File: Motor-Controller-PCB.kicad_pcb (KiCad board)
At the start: 2 copper layers, 12 parts, among them Q1 AO3401A

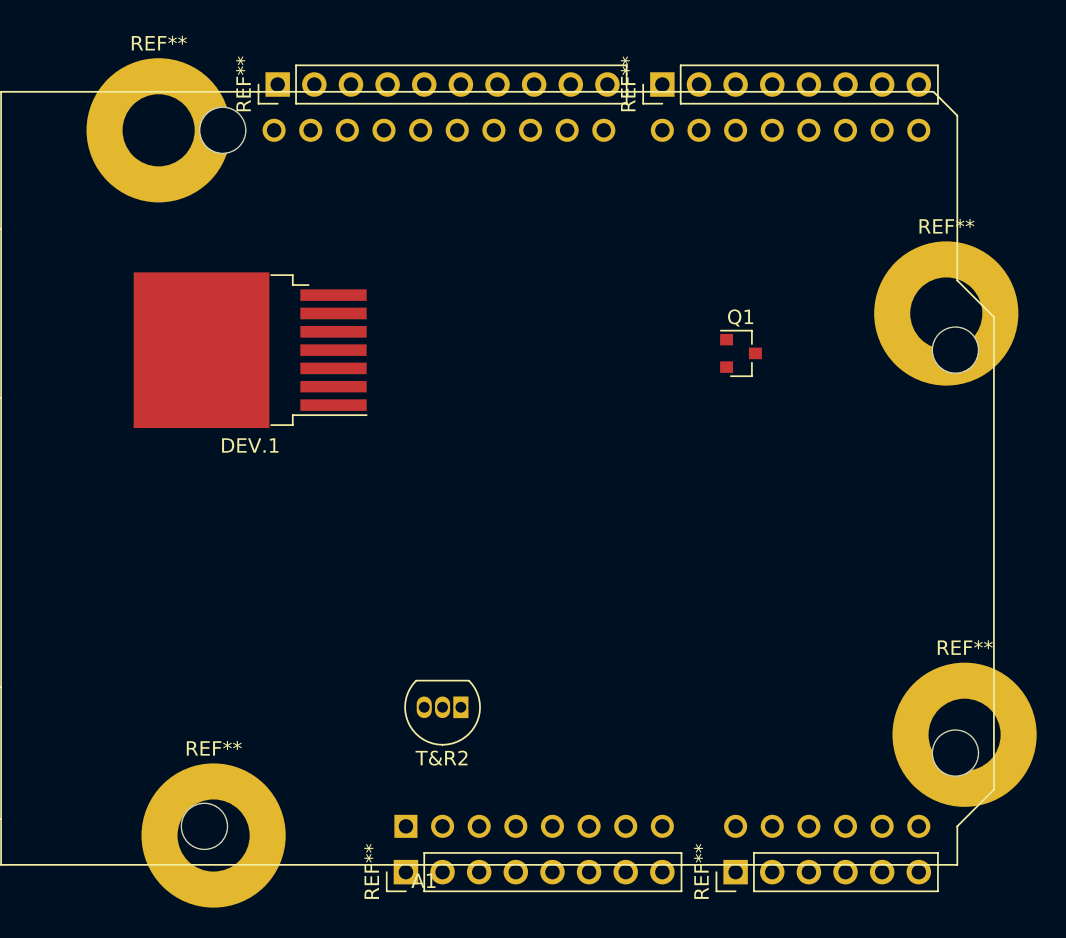
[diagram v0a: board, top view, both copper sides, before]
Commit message: Better board outline and 4mm through holes
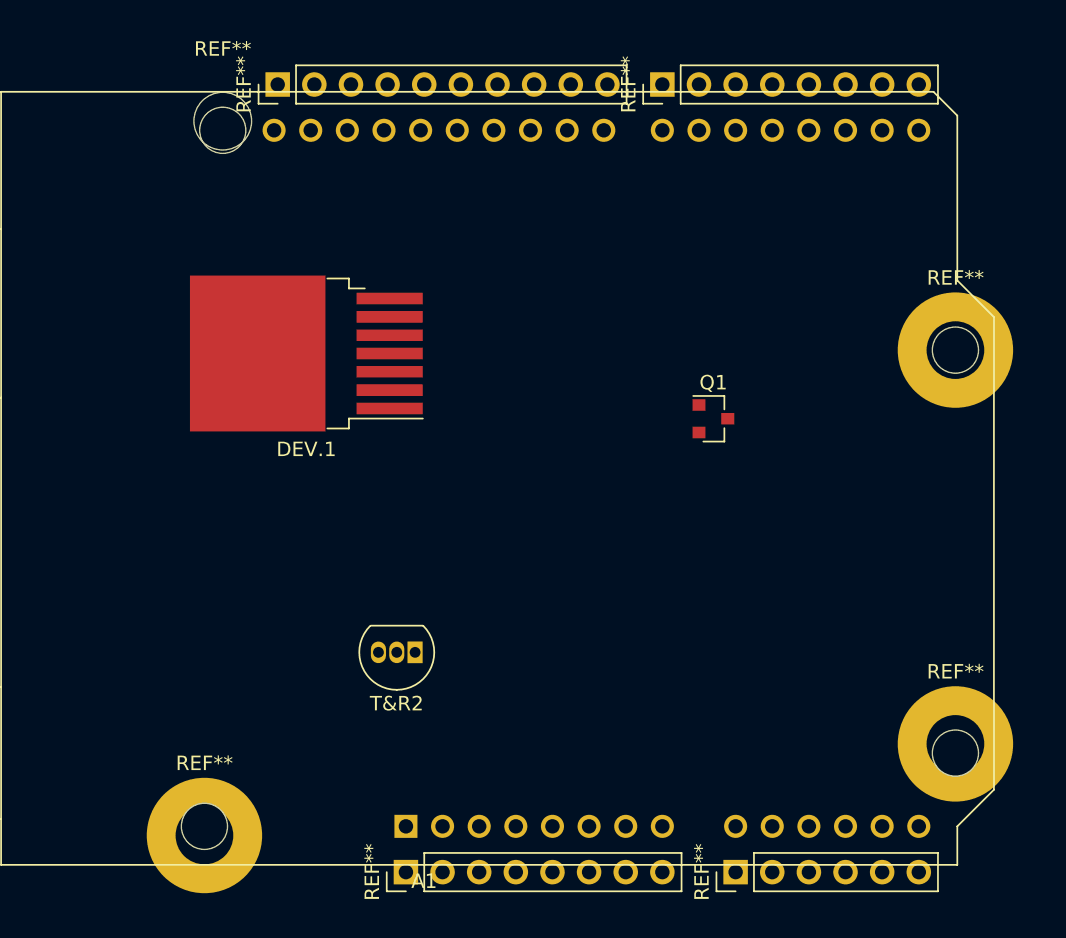
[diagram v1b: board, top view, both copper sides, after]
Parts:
- removed the REF** at (154.3, 31.1)
- removed the REF** at (158.1, 80.0)
- removed the REF** at (210.2, 73.0)
- removed the REF** at (208.9, 43.8)
- added REF**: MountingHole_4mm, MountingHole:MountingHole_4mm, F.Cu at (158.8, 30.5)
- added REF**: MountingHole_4mm_Pad, MountingHole:MountingHole_4mm_Pad, F.Cu at (157.5, 80.0)
- added REF**: MountingHole_4mm_Pad, MountingHole:MountingHole_4mm_Pad, F.Cu at (209.6, 73.7)
- added REF**: MountingHole_4mm_Pad, MountingHole:MountingHole_4mm_Pad, F.Cu at (209.6, 46.4)
- moved T&R2 4.96 mm to (172.1, 67.3)
- moved Q1 4.92 mm to (192.8, 51.1)
- moved DEV.1 3.90 mm to (164.6, 46.6)

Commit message: layouting
almost done
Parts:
- removed REF**: MountingHole_4mm, MountingHole:MountingHole_4mm
- removed REF** (x3): MountingHole_4mm_Pad, MountingHole:MountingHole_4mm_Pad
- removed REF**: PinHeader_1x06_P2.54mm_Vertical, Connector_PinHeader_2.54mm:PinHeader_1x06_P2.54mm_Vertical
- removed REF** (x2): PinHeader_1x08_P2.54mm_Vertical, Connector_PinHeader_2.54mm:PinHeader_1x08_P2.54mm_Vertical
- removed REF**: PinHeader_1x10_P2.54mm_Vertical, Connector_PinHeader_2.54mm:PinHeader_1x10_P2.54mm_Vertical
- added C10: 1nF, Capacitor_SMD:C_0805_2012Metric, B.Cu at (132.0, 102.0)
- added C11: 100nF, Capacitor_SMD:C_0805_2012Metric, B.Cu at (145.0, 116.0)
- added C12: 100uF, Capacitor_SMD:C_0805_2012Metric, B.Cu at (140.0, 96.0)
- added C14: 100nF, Capacitor_SMD:C_0805_2012Metric, B.Cu at (166.0, 94.0)
- added C4: 50V & 1500u, Capacitor_THT:CP_Radial_D18.0mm_P7.50mm, F.Cu at (163.5, 105.0)
- added C5: 220nF, Capacitor_SMD:C_0805_2012Metric, B.Cu at (145.3, 92.9)
- added C6: 220nF, Capacitor_SMD:C_0805_2012Metric, B.Cu at (156.7, 92.9)
- added D2: ZMY39, Diode_SMD:D_MELF, B.Cu at (171.0, 94.0)
- added D3: BZV55-C10, Diode_SMD:D_MiniMELF, B.Cu at (145.0, 106.0)
- added R1: 10K, Resistor_SMD:R_0805_2012Metric, B.Cu at (174.0, 76.0)
- added R12: 4.7K, Resistor_SMD:R_0805_2012Metric, B.Cu at (127.0, 86.0)
- added R13: 10K, Resistor_SMD:R_0805_2012Metric, B.Cu at (127.0, 109.0)
- added R14: 1K, Resistor_SMD:R_0805_2012Metric, B.Cu at (138.0, 116.0)
- added R15: 10K, Resistor_SMD:R_0805_2012Metric, B.Cu at (143.0, 101.0)
- added R5: 10K, Resistor_SMD:R_0805_2012Metric, B.Cu at (182.0, 85.0)
- added R7: 1K, Resistor_SMD:R_0805_2012Metric, B.Cu at (127.0, 102.1)
- added R9: 470, Resistor_SMD:R_0805_2012Metric, B.Cu at (141.5, 116.0)
- A1, DEV.1, Q1, T&R2: moved to B.Cu
- moved Q1 74.1 mm to (138.0, 101.0), turned to 90 degrees
- moved A1 58.2 mm to (184.2, 123.5), turned to 180 degrees
- moved T&R2 43.0 mm to (132.0, 83.0), turned to 90 degrees
- moved DEV.1 37.4 mm to (154.9, 82.7)
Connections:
- net Net-(C5-Pad2) renamed OUT_1
- DEV.1 pad 7: Net-(C1-Pad2) -> Net-(C14-Pad1)
- Q1 pad 2: GNDREF -> Net-(C14-Pad1)
- Q1 pad 3: VS -> VBAT
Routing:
- net GNDREF: track 0.00 -> 257.0 mm
- net Net-(A1-Pad27): track 0.00 -> 192.0 mm
- net 5V_ARDUINO: track 0.00 -> 101.6 mm
- net Net-(A1-Pad9): track 0.00 -> 100.6 mm
- net Net-(C14-Pad1): track 0.00 -> 81.8 mm
- net Net-(C11-Pad1): track 0.00 -> 73.8 mm
- net Net-(A1-Pad18): track 0.00 -> 50.9 mm
- net OUT_1: track 0.00 -> 33.1 mm
- net Net-(A1-Pad12): track 0.00 -> 30.7 mm
- net VBAT: track 0.00 -> 24.8 mm
- net Net-(DEV.1-Pad3): track 0.00 -> 24.0 mm
- net Net-(DEV.1-Pad2): track 0.00 -> 14.7 mm
- net Net-(D3-Pad2): track 0.00 -> 9.22 mm
- net Net-(R12-Pad1): track 0.00 -> 6.98 mm
- net Net-(A1-Pad31): track 0.00 -> 2.54 mm
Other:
- rule pad_to_mask_clearance: 0 -> 0.0508
- rule via_min_size: 0.4 -> 0.5

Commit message: Update Motor-Controller-PCB.kicad_pcb
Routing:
- added copper zone on B.Cu, net GNDREF
- added copper zone on F.Cu, net GNDREF

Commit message: board
giant green circles
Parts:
- added Q1: TO-252-2, Package_TO_SOT_SMD:TO-252-2, B.Cu at (167.6, 83.4)
- added REF**: Giant_Green_Circle, Motor-Controller-PCB:Giant_Green_Circle, F.Cu at (123.9, 102.8)
- added REF**: Giant_Green_Circle, Motor-Controller-PCB:Giant_Green_Circle, F.Cu at (178.6, 79.0)
- added REF**: Giant_Green_Circle, Motor-Controller-PCB:Giant_Green_Circle, F.Cu at (175.8, 118.2)
- added REF**: Giant_Green_Circle, Motor-Controller-PCB:Giant_Green_Circle, F.Cu at (124.2, 82.6)
- C6: moved to F.Cu
- moved C11 29.0 mm to (149.6, 87.4), turned to 0 degrees
- moved R9 27.6 mm to (149.5, 89.6), turned to 180 degrees
- moved C4 25.4 mm to (149.8, 83.6), turned to 0 degrees
- moved R7 23.8 mm to (149.5, 94.2), turned to 180 degrees
- moved C12 23.1 mm to (121.5, 109.7)
- moved C10 20.2 mm to (149.4, 91.8), turned to 180 degrees
- moved R5 19.2 mm to (165.2, 75.8)
- moved C6 17.5 mm to (142.0, 83.4)
- moved DEV.1 17.3 mm to (138.2, 87.0)
- moved T&R2 12.7 mm to (134.7, 95.4), turned to 0 degrees
- moved C5 9.31 mm to (150.2, 100.8)
- moved R12 2.93 mm to (125.7, 88.6)
- moved R1 2.00 mm to (172.0, 75.9)
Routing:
- net GNDREF: track 257.0 -> 52.4 mm, vias 0 -> 6
- net Net-(C11-Pad1): track 73.8 -> 7.39 mm
- net 5V_ARDUINO: track 101.6 -> 68.3 mm
- net OUT_1: track 33.1 -> 8.29 mm
- net Net-(DEV.1-Pad3): track 24.0 -> 0.00 mm
- net Net-(DEV.1-Pad2): track 14.7 -> 0.00 mm
- net VBAT: track 24.8 -> 10.7 mm
- net Net-(A1-Pad9): track 100.6 -> 92.7 mm
- net Net-(R12-Pad1): track 6.98 -> 0.00 mm
- net Net-(A1-Pad18): track 50.9 -> 46.1 mm
- net Net-(C14-Pad1): track 81.8 -> 86.3 mm
- net Net-(A1-Pad27): track 192.0 -> 190.5 mm
- removed copper zone on B.Cu, net GNDREF
- removed copper zone on F.Cu, net GNDREF

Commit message: layouting
layouting
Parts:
- removed the Q1 at (167.6, 83.4)
- removed the Q1 at (138.0, 101.0)
- removed the REF** at (123.9, 102.8)
- removed the REF** at (178.6, 79.0)
- removed the REF** at (175.8, 118.2)
- removed the REF** at (124.2, 82.6)
- added Q1: IPD90P04P4L, Motor-Controller-PCB:TO-252-3_TabPin2, B.Cu at (170.2, 90.1)
- added REF**: Giant_Green_Circle, Motor-Controller-PCB:Giant_Green_Circle, F.Cu at (122.8, 105.2)
- added REF**: Giant_Green_Circle, Motor-Controller-PCB:Giant_Green_Circle, F.Cu at (175.8, 115.5)
- added REF**: Giant_Green_Circle, Motor-Controller-PCB:Giant_Green_Circle, F.Cu at (177.5, 80.0)
- added REF**: Giant_Green_Circle, Motor-Controller-PCB:Giant_Green_Circle, F.Cu at (124.6, 84.1)
- moved C12 56.2 mm to (176.9, 118.9), turned to 0 degrees
- moved R1 40.9 mm to (131.1, 74.9), turned to 180 degrees
- moved R15 30.4 mm to (173.4, 100.3), turned to 0 degrees
- moved R13 28.9 mm to (154.9, 116.5)
- moved C5 28.0 mm to (122.9, 94.7), turned to 90 degrees
- moved D3 27.1 mm to (170.8, 97.7), turned to 0 degrees
- moved R12 25.3 mm to (136.9, 111.3), turned to 0 degrees
- moved C14 15.9 mm to (160.6, 79.0)
- moved D2 15.0 mm to (164.4, 80.5)
- moved R14 12.5 mm to (125.5, 117.3), turned to 90 degrees
- moved R5 12.0 mm to (153.5, 78.5), turned to 270 degrees
- moved A1 0.25 mm to (184.0, 123.5)
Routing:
- net Net-(A1-Pad27): track 190.5 -> 5.29 mm
- net Net-(A1-Pad18): track 46.1 -> 3.77 mm
- net GNDREF: track 52.4 -> 83.5 mm, vias 6 -> 12
- net VBAT: track 10.7 -> 37.6 mm
- net Net-(A1-Pad9): track 92.7 -> 68.4 mm
- net Net-(DEV.1-Pad2): track 0.00 -> 22.3 mm
- net Net-(R12-Pad1): track 0.00 -> 15.9 mm
- net Net-(DEV.1-Pad3): track 0.00 -> 14.3 mm
- net Net-(A1-Pad12): track 30.7 -> 37.4 mm
- net Net-(C14-Pad1): track 86.3 -> 89.6 mm
- net Net-(D3-Pad2): track 9.22 -> 6.03 mm
- net OUT_1: track 8.29 -> 10.5 mm
- net 5V_ARDUINO: track 68.3 -> 69.0 mm
- added copper zone on B.Cu, net GNDREF
- added copper zone on F.Cu, net GNDREF
- added copper zone on B.Cu, net Net-(C14-Pad1)
- added copper zone on B.Cu, net OUT_1
- added copper zone on F.Cu, net OUT_1
- added copper zone on B.Cu, net VBAT
- added copper zone on F.Cu, net VBAT

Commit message: layouting
layouting
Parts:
- C12: footprint Capacitor_SMD:C_0805_2012Metric -> Capacitor_SMD:CP_Elec_10x10; moved to F.Cu
- C6: moved to B.Cu
- D2: value ZMY39 -> 1N4754A; footprint Diode_SMD:D_MELF -> Diode_THT:D_DO-41_SOD81_P10.16mm_Horizontal; moved to F.Cu
- moved C12 28.1 mm to (178.7, 90.8), turned to 90 degrees
- moved C4 14.3 mm to (149.3, 97.9)
- moved C6 8.41 mm to (149.9, 86.2)
- moved D2 4.65 mm to (164.4, 75.8)
- moved T&R2 3.20 mm to (134.7, 98.6)
- moved C11 0.96 mm to (149.9, 88.3)
- moved R9 0.89 mm to (149.9, 90.4)
- moved C10 0.80 mm to (149.9, 92.4)
- moved R7 0.52 mm to (149.9, 94.5)
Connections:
- A1 pad 32: Net-(A1-Pad31) -> Net-(A1-Pad32)
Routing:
- net Net-(C14-Pad1): track 89.6 -> 58.6 mm
- net GNDREF: track 83.5 -> 59.6 mm
- net Net-(R12-Pad1): track 15.9 -> 12.7 mm
- net Net-(A1-Pad9): track 68.4 -> 71.5 mm
- net OUT_1: track 10.5 -> 13.2 mm
- net Net-(A1-Pad31): track 2.54 -> 0.00 mm
- net Net-(C11-Pad1): track 7.39 -> 9.55 mm
- net VBAT: track 37.6 -> 35.6 mm

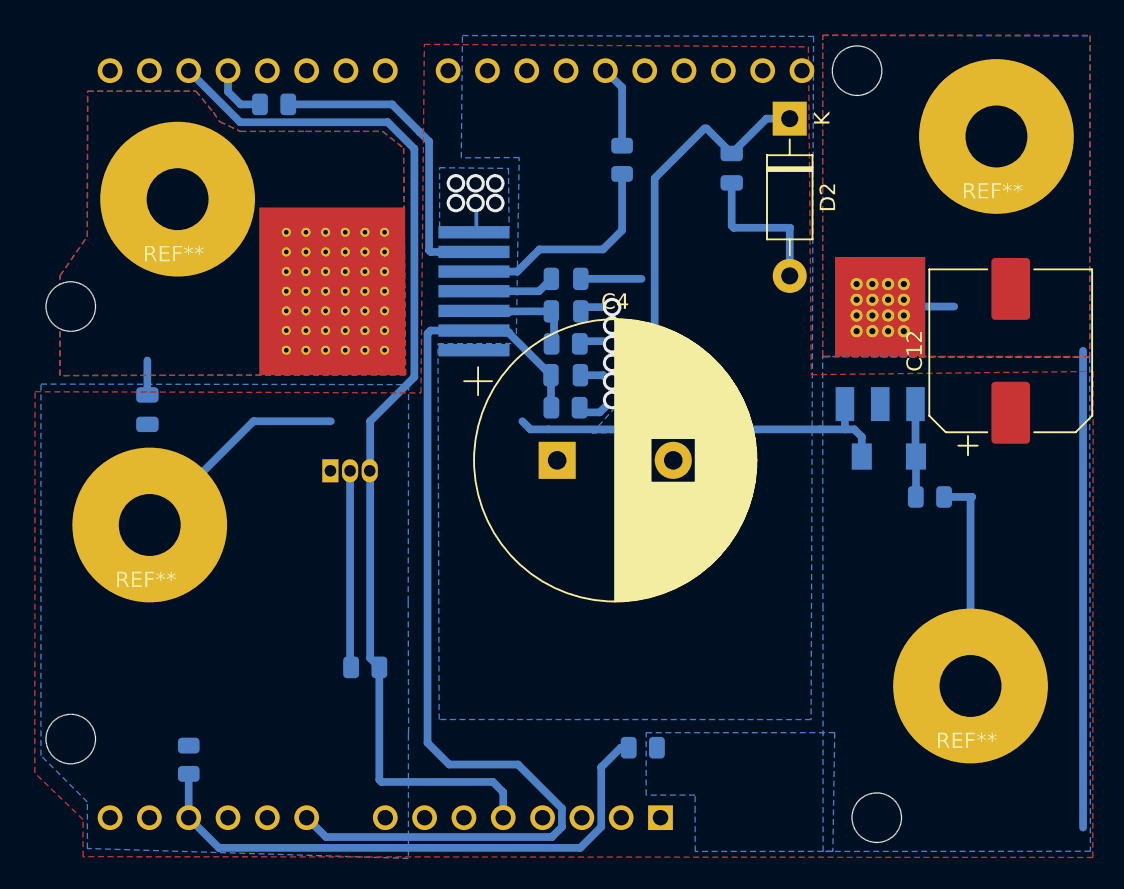
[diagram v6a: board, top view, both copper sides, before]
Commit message: New parts and schematic cleanup
Co-Authored-By: William <28985448+wzhouiup@users.noreply.github.com>
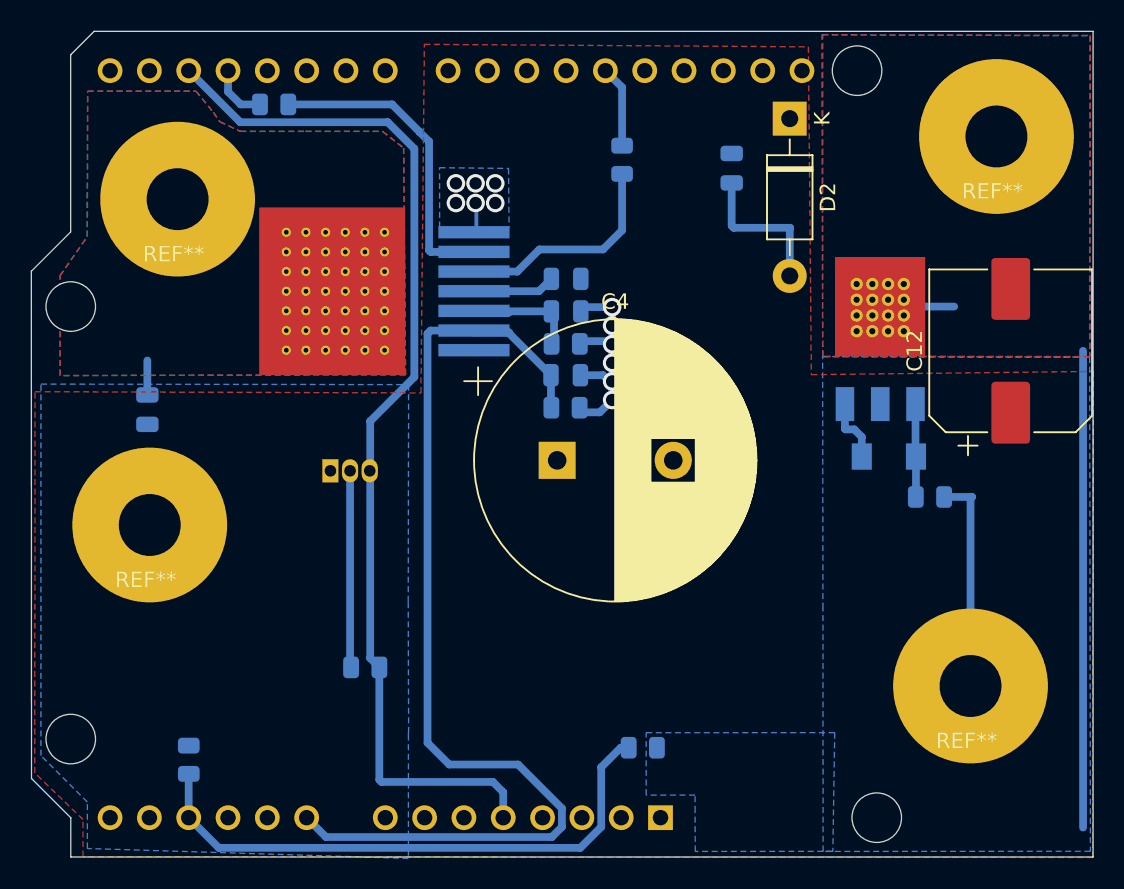
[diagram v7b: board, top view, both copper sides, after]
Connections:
- net GNDREF renamed GND
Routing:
- net Net-(C14-Pad1): track 58.6 -> 5.35 mm
- net GND: track 59.6 -> 45.1 mm
- removed copper zone on B.Cu, net Net-(C14-Pad1)
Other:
- board outline added: 68.6 x 53.3 mm
- net class Default: clearance 0.2 -> 0.1524; trace_width 0.25 -> 0.1524; via_dia 0.8 -> 0.508; via_drill 0.4 -> 0.254
- rule trace_clearance: 0.2 -> 0.1524
- rule trace_min: 0.2 -> 0.1524
- rule via_min_drill: 0.3 -> 0.254
- rule via_min_size: 0.5 -> 0.508

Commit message: layouting
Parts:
- removed C10: 1nF, Capacitor_SMD:C_0805_2012Metric
- removed C12: 100uF, Capacitor_SMD:CP_Elec_10x10
- removed DEV.1: BTN8982TA, Package_TO_SOT_SMD:TO-263-7_TabPin8
- removed R12: 4.7K, Resistor_SMD:R_0805_2012Metric
- removed R7: 1K, Resistor_SMD:R_0805_2012Metric
- removed R9: 470, Resistor_SMD:R_0805_2012Metric
- removed T&R2: DS18B20, Package_TO_SOT_THT:TO-92_Inline
- added C1: 10nF, Capacitor_SMD:C_0805_2012Metric_Pad1.18x1.45mm_HandSolder, B.Cu at (130.6, 117.5)
- added C11: 100nF, Capacitor_SMD:C_0805_2012Metric_Pad1.18x1.45mm_HandSolder, B.Cu at (149.4, 90.5)
- added C14: 100nF, Capacitor_SMD:C_0805_2012Metric_Pad1.18x1.45mm_HandSolder, B.Cu at (160.5, 86.6)
- added C2: 1µF, Capacitor_SMD:C_0805_2012Metric_Pad1.18x1.45mm_HandSolder, B.Cu at (160.9, 94.5)
- added C5: 220nF, Capacitor_SMD:C_0805_2012Metric_Pad1.18x1.45mm_HandSolder, B.Cu at (120.7, 94.8)
- added C6: 220nF, Capacitor_SMD:C_0805_2012Metric_Pad1.18x1.45mm_HandSolder, B.Cu at (149.9, 83.8)
- added C7: 100µF, Capacitor_SMD:CP_Elec_10x10, B.Cu at (168.3, 105.0)
- added D1: 10V, Diode_SMD:D_MiniMELF, B.Cu at (163.1, 97.7)
- added Q2: TJ200F04M3L, Motor-Controller-PCB:TO-220SM-3_TabPin2_ThermalVias, B.Cu at (161.0, 107.8)
- added Q3: TJ200F04M3L, Motor-Controller-PCB:TO-220SM-3_TabPin2_ThermalVias, B.Cu at (171.9, 95.1)
- added R2: 20k, Resistor_SMD:R_0805_2012Metric_Pad1.20x1.40mm_HandSolder, B.Cu at (140.6, 95.2)
- added R3: 100, Resistor_SMD:R_0805_2012Metric_Pad1.20x1.40mm_HandSolder, B.Cu at (159.6, 114.8)
- added R4: 10M, Resistor_SMD:R_0805_2012Metric_Pad1.20x1.40mm_HandSolder, B.Cu at (168.0, 116.2)
- added U1: DS18B20-PAR, Package_TO_SOT_THT:TO-92_Inline, B.Cu at (134.7, 98.6)
- C4: value 50V & 1500u -> 50V 1500µF
- D2: value 1N4754A -> 39V; moved to B.Cu
- D3: value BZV55-C10 -> 10V
- Q1: value IPD90P04P4L -> IFX007T; footprint Motor-Controller-PCB:TO-252-3_TabPin2 -> Package_TO_SOT_SMD:TO-263-7_TabPin8
- R1, R13, R15, R5: value 10K -> 10k; footprint Resistor_SMD:R_0805_2012Metric -> Resistor_SMD:R_0805_2012Metric_Pad1.20x1.40mm_HandSolder
- R14: value 1K -> 1.47k; footprint Resistor_SMD:R_0805_2012Metric -> Resistor_SMD:R_0805_2012Metric_Pad1.20x1.40mm_HandSolder
- moved Q1 32.2 mm to (138.2, 87.0), turned to 180 degrees
- moved R14 23.9 mm to (149.4, 117.8), turned to 180 degrees
- moved D2 18.5 mm to (164.2, 94.3), turned to 90 degrees
- moved REF** 7.70 mm to (122.5, 112.8)
- moved R15 5.63 mm to (174.8, 105.8), turned to 270 degrees
- moved C14 5.30 mm to (160.5, 84.3), turned to 0 degrees
- moved C4 3.95 mm to (152.9, 96.2), turned to 90 degrees
- moved R5 3.92 mm to (151.4, 75.2), turned to 0 degrees
- moved REF** 3.38 mm to (177.1, 118.6)
- moved D3 2.04 mm to (172.8, 98.2)
- moved R13 1.38 mm to (154.1, 115.3), turned to 270 degrees
- moved C11 0.53 mm to (149.4, 88.3)
- moved R1 0.25 mm to (130.8, 74.8)
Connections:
- A1 pad 17: 5V_ARDUINO -> Net-(A1-Pad17)
- A1 pad 5: 5V_ARDUINO -> Net-(A1-Pad5)
- A1 pad 8: GND -> Net-(A1-Pad8)
- D2 pad 1: Net-(C14-Pad1) -> Net-(C2-Pad2)
- D3 pad 1: Net-(C14-Pad1) -> Net-(C2-Pad2)
- Q1 pad 1: Net-(D3-Pad2) -> GND
- Q1 pad 2: VBAT -> Net-(Q1-Pad2)
- Q1 pad 3: Net-(C14-Pad1) -> Net-(Q1-Pad3)
- R1 pad 1: Net-(DEV.1-Pad2) -> Net-(Q1-Pad2)
- R13 pad 1: VBAT -> Net-(C14-Pad1)
- R5 pad 1: Net-(A1-Pad27) -> Net-(Q1-Pad3)
- R5 pad 2: Net-(DEV.1-Pad3) -> Net-(A1-Pad27)
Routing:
- net Net-(A1-Pad9): track 71.5 -> 0.00 mm
- net 5V_ARDUINO: track 69.0 -> 0.00 mm
- net Net-(C2-Pad2): track 0.00 -> 42.7 mm
- net Net-(A1-Pad17): track 0.00 -> 41.4 mm
- net Net-(A1-Pad10): track 0.00 -> 38.2 mm
- net VBAT: track 35.6 -> 4.78 mm
- net Net-(C2-Pad1): track 0.00 -> 24.9 mm
- net GND: track 45.1 -> 69.8 mm, vias 12 -> 6
- net Net-(C14-Pad1): track 5.35 -> 29.6 mm
- net Net-(DEV.1-Pad2): track 22.3 -> 0.00 mm
- net Net-(Q1-Pad2): track 0.00 -> 22.3 mm
- net Net-(Q1-Pad3): track 0.00 -> 16.5 mm
- net Net-(DEV.1-Pad3): track 14.3 -> 0.00 mm
- net Net-(R12-Pad1): track 12.7 -> 0.00 mm
- net Net-(Q1-Pad6): track 0.00 -> 7.34 mm
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- added copper zone on B.Cu, net Net-(C14-Pad1)
